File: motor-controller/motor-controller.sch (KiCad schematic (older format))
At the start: 14 parts, among them J1 Molex 172043-0201 R/A, J2 Molex 172043-0302 R/A, J3 MCU-IO, U1 DRV10983PWP

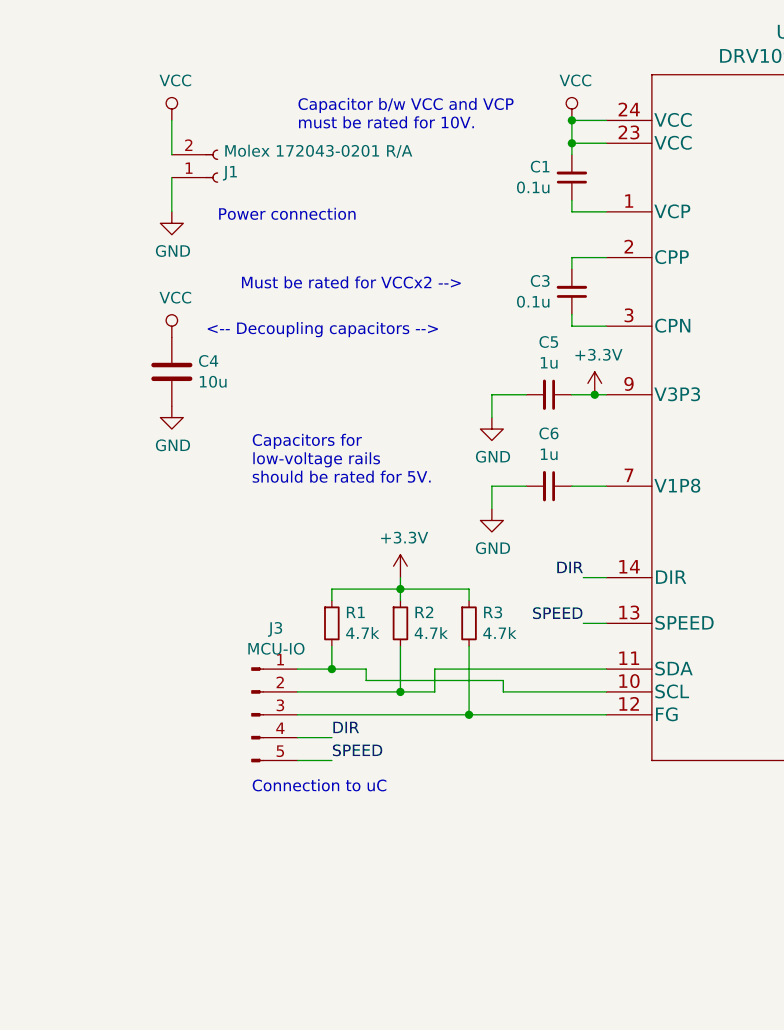
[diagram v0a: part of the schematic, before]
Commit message: Added fuse holder and modified position of mounting holes
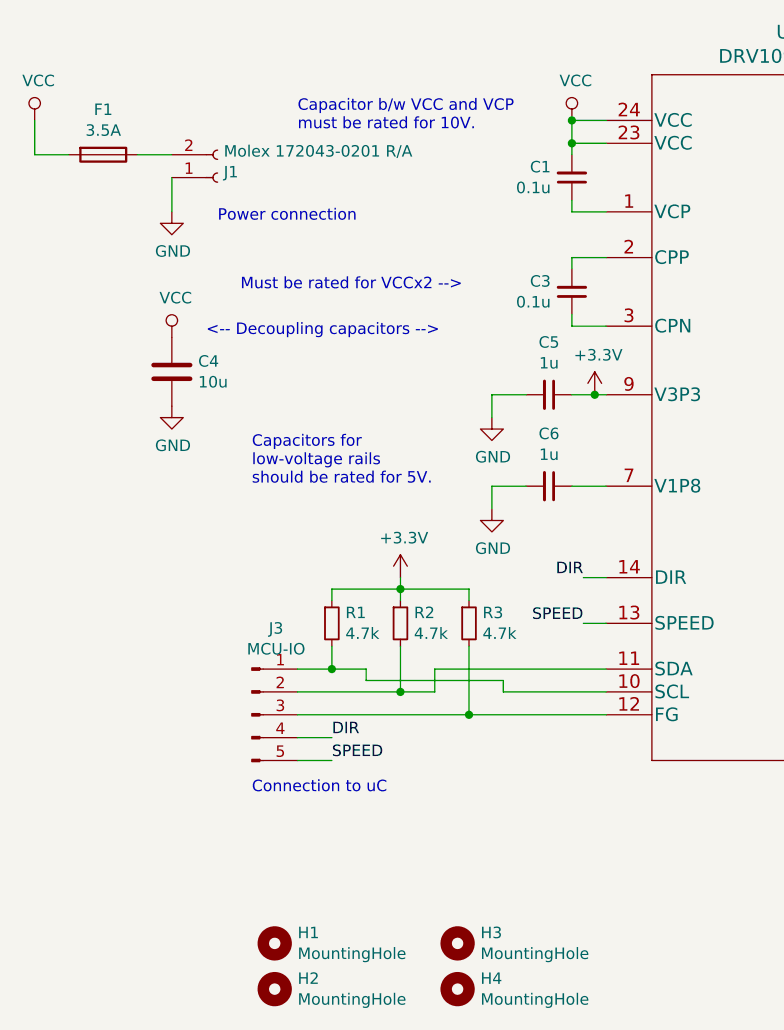
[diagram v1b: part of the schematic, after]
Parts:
- added F1: 3.5A, custom:littelfuse-01110505Z-5x15mm, symbol Device:Fuse
- added H1, H2, H3, H4: MountingHole, MountingHole:MountingHole_3.2mm_M3, symbol Mechanical:MountingHole
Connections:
- net VCC: now also F1.2; no longer J1.2 (Pin_2)
- new net: F1.1, J1.2 (Pin_2)
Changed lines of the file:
@@
 Sheet 1 1
 Title "Brushless DC Motor Controller"
-Date "2020-12-24"
-Rev "0.0.1"
+Date "2021-01-03"
+Rev "0.0.2"
 Comp "JHU Deliverbot Project"
 Comment1 ""
@@
 L power:VCC #PWR0108
 U 1 1 5FE6FEFE
-P 2950 2150
-F 0 "#PWR0108" H 2950 2000 50  0001 C CNN
-F 1 "VCC" H 2967 2323 50  0000 C CNN
-F 2 "" H 2950 2150 50  0001 C CNN
-F 3 "" H 2950 2150 50  0001 C CNN
-	1    2950 2150
+P 2350 2150
+F 0 "#PWR0108" H 2350 2000 50  0001 C CNN
+F 1 "VCC" H 2367 2323 50  0000 C CNN
+F 2 "" H 2350 2150 50  0001 C CNN
+F 3 "" H 2350 2150 50  0001 C CNN
+	1    2350 2150
 	1    0    0    -1
 $EndComp
@@
 $EndComp
 Wire Wire Line
-	2950 2150 2950 2300
+	2350 2150 2350 2300
 Wire Wire Line
 	2950 2400 2950 2550
@@
 	4400 4650 4850 4650
 Connection ~ 3650 4550
+$Comp
+L Mechanical:MountingHole H2
+U 1 1 5FF140AB
+P 3400 5950
+F 0 "H2" H 3500 5996 50  0000 L CNN
+F 1 "MountingHole" H 3500 5905 50  0000 L CNN
+F 2 "MountingHole:MountingHole_3.2mm_M3" H 3400 5950 50  0001 C CNN
+F 3 "~" H 3400 5950 50  0001 C CNN
+	1    3400 5950
+	1    0    0    -1
+$EndComp
+$Comp
+L Mechanical:MountingHole H1
+U 1 1 5FF15A3A
+P 3400 5750
+F 0 "H1" H 3500 5796 50  0000 L CNN
+F 1 "MountingHole" H 3500 5705 50  0000 L CNN
+F 2 "MountingHole:MountingHole_3.2mm_M3" H 3400 5750 50  0001 C CNN
+F 3 "~" H 3400 5750 50  0001 C CNN
+	1    3400 5750
+	1    0    0    -1
+$EndComp
+$Comp
+L Mechanical:MountingHole H4
+U 1 1 5FF29E21
+P 4200 5950
+F 0 "H4" H 4300 5996 50  0000 L CNN
+F 1 "MountingHole" H 4300 5905 50  0000 L CNN
+F 2 "MountingHole:MountingHole_3.2mm_M3" H 4200 5950 50  0001 C CNN
+F 3 "~" H 4200 5950 50  0001 C CNN
+	1    4200 5950
+	1    0    0    -1
+$EndComp
+$Comp
+L Mechanical:MountingHole H3
+U 1 1 5FF29E28
+P 4200 5750
+F 0 "H3" H 4300 5796 50  0000 L CNN
+F 1 "MountingHole" H 4300 5705 50  0000 L CNN
+F 2 "MountingHole:MountingHole_3.2mm_M3" H 4200 5750 50  0001 C CNN
+F 3 "~" H 4200 5750 50  0001 C CNN
+	1    4200 5750
+	1    0    0    -1
+$EndComp
+$Comp
+L Device:Fuse F1
+U 1 1 5FF2D941
+P 2650 2300
+F 0 "F1" V 2453 2300 50  0000 C CNN
+F 1 "3.5A" V 2544 2300 50  0000 C CNN
+F 2 "custom:littelfuse-01110505Z-5x15mm" V 2580 2300 50  0001 C CNN
+F 3 "~" H 2650 2300 50  0001 C CNN
+F 4 "https://www.digikey.com/en/products/detail/littelfuse-inc/022503-5MXP/777791" V 2650 2300 50  0001 C CNN "Fuse"
+F 5 "https://www.digikey.com/en/products/detail/littelfuse-inc/01110505Z/2518624" V 2650 2300 50  0001 C CNN "Holder"
+	1    2650 2300
+	0    1    1    0
+$EndComp
+Wire Wire Line
+	2350 2300 2500 2300
+Wire Wire Line
+	2800 2300 2950 2300
 $EndSCHEMATC
